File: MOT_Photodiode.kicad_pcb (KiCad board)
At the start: 2 copper layers, 32 x 25 mm, 18 parts, among them J1 Supply, J2 output, J3 photodiode, U1 LT3032-12, U2 ADA4898-1YRDZ

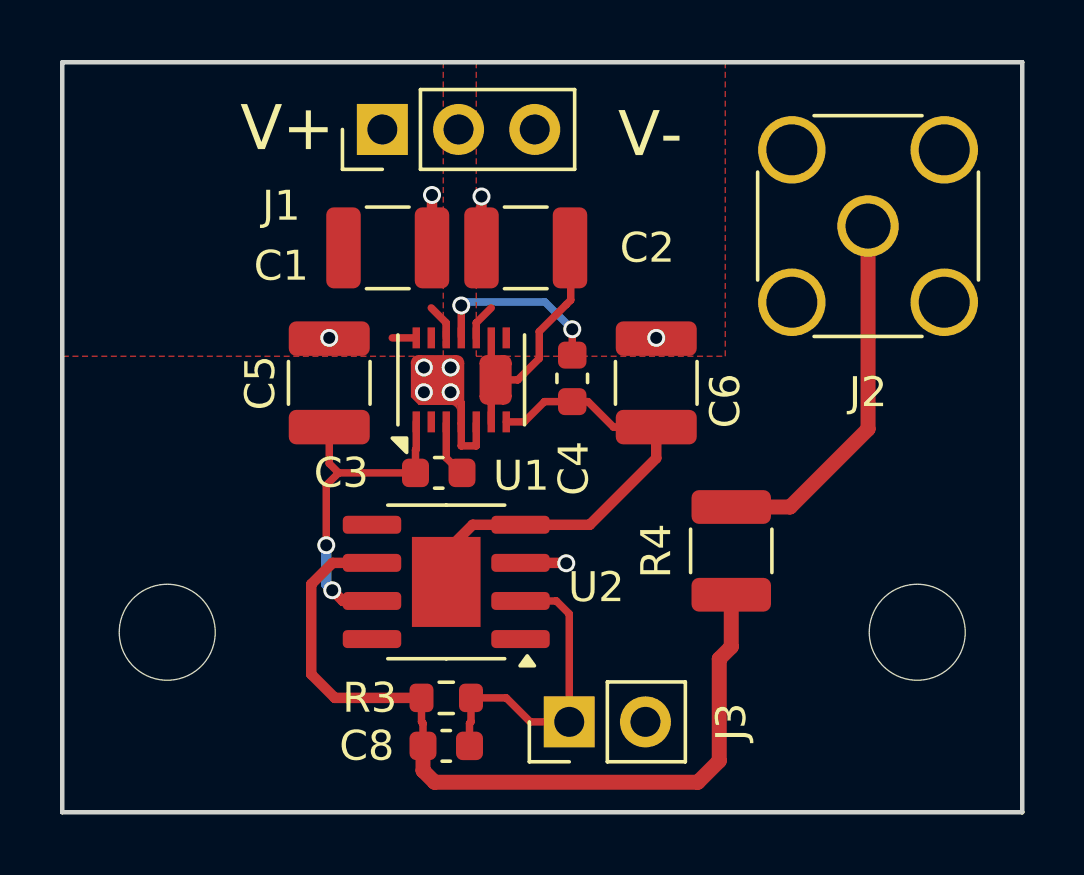
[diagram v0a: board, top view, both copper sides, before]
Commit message: Reduced via drill size from 0.4 mm to 0.3 mm
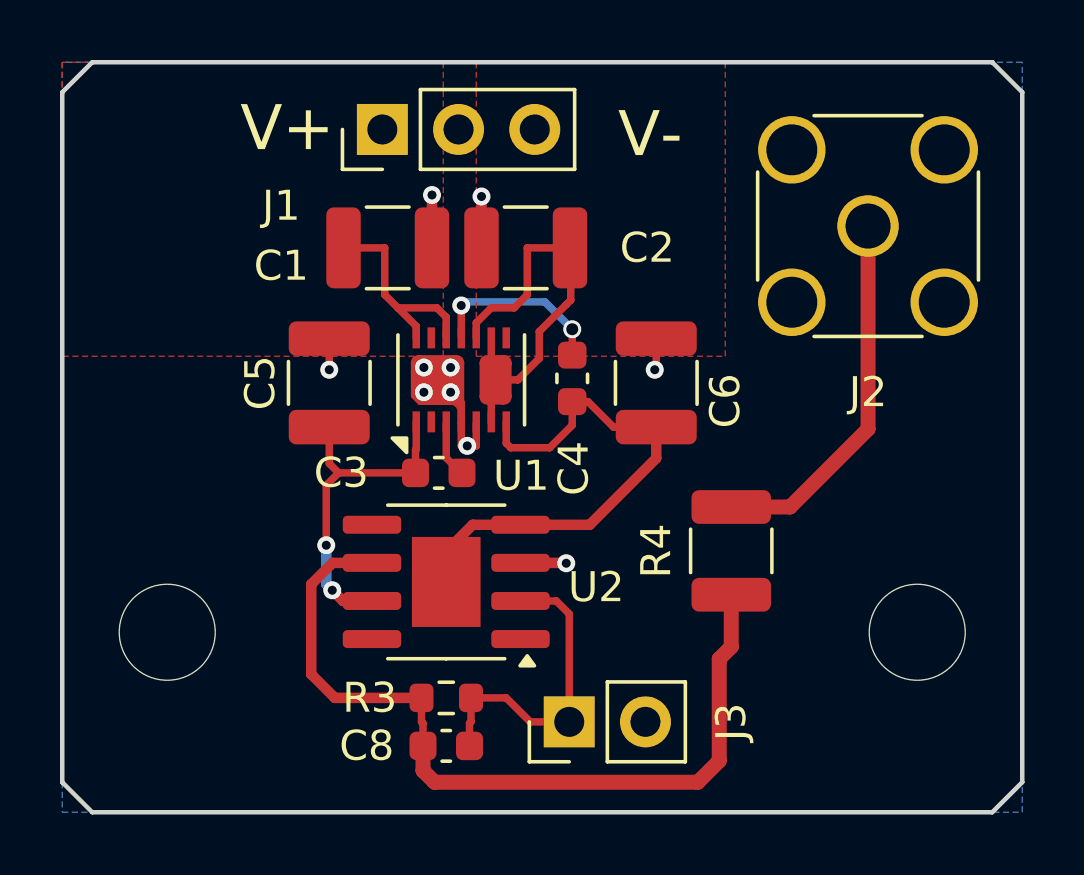
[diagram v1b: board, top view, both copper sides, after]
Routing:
- net +15V: track 2.01 -> 7.24 mm
- net -15V: track 8.37 -> 12.7 mm
- net GND: track 8.19 -> 10.3 mm, vias 9 -> 10
- net V-: track 16.0 -> 17.6 mm
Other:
- outline, holes or cut-outs redrawn
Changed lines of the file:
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@@
 	)
 	(gr_line
-		(start 127.45 112.25)
-		(end 159.45 112.25)
+		(start 128.45 112.25)
+		(end 158.45 112.25)
 		(stroke
 			(width 0.15)
@@
 	)
 	(gr_line
-		(start 159.45 112.25)
-		(end 159.45 87.25)
+		(start 159.45 111.25)
+		(end 159.45 88.25)
 		(stroke
 			(width 0.15)
@@
 	)
 	(gr_line
-		(start 159.45 87.25)
-		(end 127.45 87.25)
+		(start 159.45 88.25)
+		(end 158.45 87.25)
+		(stroke
+			(width 0.15)
+			(type default)
+		)
+		(layer "Edge.Cuts")
+	)
+	(gr_line
+		(start 158.45 87.25)
+		(end 128.45 87.25)
 		(stroke
 			(width 0.15)
@@
 	)
 	(gr_line
-		(start 127.45 87.25)
-		(end 127.45 112.25)
+		(start 127.45 88.25)
+		(end 127.45 111.25)
 		(stroke
 			(width 0.15)
 			(type solid)
+		)
+		(layer "Edge.Cuts")
+	)
+	(gr_line
+		(start 127.45 88.25)
+		(end 128.45 87.25)
+		(stroke
+			(width 0.15)
+			(type default)
+		)
+		(layer "Edge.Cuts")
+	)
+	(gr_line
+		(start 158.45 112.25)
+		(end 159.45 111.25)
+		(stroke
+			(width 0.15)
+			(type default)
+		)
+		(layer "Edge.Cuts")
+	)
+	(gr_line
+		(start 128.45 112.25)
+		(end 127.45 111.25)
+		(stroke
+			(width 0.15)
+			(type default)
 		)
 		(layer "Edge.Cuts")
@@
 	)
 	(segment
+		(start 147.2 97.5)
+		(end 147.25 97.45)
+		(width 0.25)
+		(layer "F.Cu")
+		(net 1)
+	)
+	(segment
+		(start 140.95 100.0375)
+		(end 141.25 100.0375)
+		(width 0.25)
+		(layer "F.Cu")
+		(net 1)
+	)
+	(segment
 		(start 140.75 99.2875)
 		(end 140.75 98.605)
@@
 	)
 	(segment
+		(start 147.25 97.45)
+		(end 147.25 96.4625)
+		(width 0.25)
+		(layer "F.Cu")
+		(net 1)
+	)
+	(segment
 		(start 144.2375 103.9375)
 		(end 144.25 103.95)
@@
 	)
 	(segment
+		(start 136.35 96.4625)
+		(end 136.35 97.5)
+		(width 0.25)
+		(layer "F.Cu")
+		(net 1)
+	)
+	(segment
 		(start 141.425 91.725)
 		(end 141.425 93.4375)
@@
 	(segment
 		(start 140.75 100.0375)
-		(end 141.25 100.0375)
+		(end 140.95 100.0375)
 		(width 0.25)
 		(layer "F.Cu")
@@
 		(at 139.505 97.425)
 		(size 0.6)
-		(drill 0.4)
+		(drill 0.3)
 		(layers "F.Cu" "B.Cu")
 		(net 1)
@@
 		(at 139.505 98.25)
 		(size 0.6)
-		(drill 0.4)
+		(drill 0.3)
 		(layers "F.Cu" "B.Cu")
 		(net 1)
@@
 		(at 144.25 103.95)
 		(size 0.6)
-		(drill 0.4)
+		(drill 0.3)
 		(layers "F.Cu" "B.Cu")
 		(net 1)
@@
 		(at 140.395 97.425)
 		(size 0.6)
-		(drill 0.4)
-		(layers "F.Cu" "B.Cu")
-		(net 1)
-	)
-	(via
-		(at 136.35 96.4375)
-		(size 0.6)
-		(drill 0.4)
+		(drill 0.3)
+		(layers "F.Cu" "B.Cu")
+		(net 1)
+	)
+	(via
+		(at 136.35 97.5)
+		(size 0.6)
+		(drill 0.3)
 		(layers "F.Cu" "B.Cu")
 		(net 1)
@@
 		(at 141.425 91.725)
 		(size 0.6)
-		(drill 0.4)
+		(drill 0.3)
+		(layers "F.Cu" "B.Cu")
+		(net 1)
+	)
+	(via
+		(at 140.95 100.0375)
+		(size 0.6)
+		(drill 0.3)
 		(layers "F.Cu" "B.Cu")
 		(net 1)
@@
 		(at 140.395 98.25)
 		(size 0.6)
-		(drill 0.4)
+		(drill 0.3)
 		(layers "F.Cu" "B.Cu")
 		(net 1)
@@
 		(at 139.775 91.675)
 		(size 0.6)
-		(drill 0.4)
-		(layers "F.Cu" "B.Cu")
-		(net 1)
-	)
-	(via
-		(at 147.25 96.4375)
-		(size 0.6)
-		(drill 0.4)
+		(drill 0.3)
+		(layers "F.Cu" "B.Cu")
+		(net 1)
+	)
+	(via
+		(at 147.2 97.5)
+		(size 0.6)
+		(drill 0.3)
 		(layers "F.Cu" "B.Cu")
 		(net 1)
@@
 		(at 136.45 104.85)
 		(size 0.6)
-		(drill 0.4)
+		(drill 0.3)
 		(layers "F.Cu" "B.Cu")
 		(net 2)
@@
 		(at 136.25 103.35)
 		(size 0.6)
-		(drill 0.4)
+		(drill 0.3)
 		(layers "F.Cu" "B.Cu")
 		(net 2)
@@
 	(segment
 		(start 142.25 99.2375)
-		(end 142.85 99.2375)
+		(end 142.25 99.95)
+		(width 0.25)
+		(layer "F.Cu")
+		(net 3)
+	)
+	(segment
+		(start 142.25 99.95)
+		(end 142.4 100.1)
+		(width 0.25)
+		(layer "F.Cu")
+		(net 3)
+	)
+	(segment
+		(start 143.7 100.1)
+		(end 144.45 99.35)
 		(width 0.25)
 		(layer "F.Cu")
@@
 	)
 	(segment
-		(start 142.85 99.2375)
-		(end 143.525 98.5625)
-		(width 0.25)
-		(layer "F.Cu")
-		(net 3)
-	)
-	(segment
 		(start 141.1325 102.6675)
 		(end 140.25 103.55)
@@
 	)
 	(segment
+		(start 144.45 99.35)
+		(end 144.45 98.5625)
+		(width 0.25)
+		(layer "F.Cu")
+		(net 3)
+	)
+	(segment
 		(start 147.25 100.45)
 		(end 147.25 99.4125)
@@
 	)
 	(segment
-		(start 143.525 98.5625)
-		(end 144.45 98.5625)
+		(start 142.4 100.1)
+		(end 143.7 100.1)
 		(width 0.25)
 		(layer "F.Cu")
@@
 		(at 140.75 95.357825)
 		(size 0.6)
-		(drill 0.4)
+		(drill 0.3)
 		(layers "F.Cu" "B.Cu")
 		(net 6)
@@
 	)
 	(segment
+		(start 140.25 95.75)
+		(end 139.9375 95.4375)
+		(width 0.25)
+		(layer "F.Cu")
+		(net 13)
+	)
+	(segment
 		(start 140.25 96.4375)
-		(end 140.25 95.9375)
+		(end 140.25 95.75)
 		(width 0.25)
 		(layer "F.Cu")
@@
 	)
 	(segment
-		(start 140.25 95.9375)
-		(end 139.75 95.4375)
+		(start 138.2 95)
+		(end 138.2 93.4375)
 		(width 0.25)
 		(layer "F.Cu")
@@
 	)
 	(segment
+		(start 138.2 93.4375)
+		(end 136.825 93.4375)
+		(width 0.25)
+		(layer "F.Cu")
+		(net 13)
+	)
+	(segment
+		(start 139.25 96.05)
+		(end 138.2 95)
+		(width 0.25)
+		(layer "F.Cu")
+		(net 13)
+	)
+	(segment
 		(start 139.25 96.4375)
-		(end 138.45 96.4375)
+		(end 139.25 96.05)
+		(width 0.25)
+		(layer "F.Cu")
+		(net 13)
+	)
+	(segment
+		(start 139.9375 95.4375)
+		(end 138.6375 95.4375)
 		(width 0.25)
 		(layer "F.Cu")
@@
 	)
 	(segment
+		(start 142.5125 95.4375)
+		(end 142.95 95)
+		(width 0.25)
+		(layer "F.Cu")
+		(net 14)
+	)
+	(segment
 		(start 144.25 95.3275)
 		(end 143.35 96.2275)
@@
 	)
 	(segment
+		(start 141.75 99.2875)
+		(end 141.75 97.9375)
+		(width 0.25)
+		(layer "F.Cu")
+		(net 14)
+	)
+	(segment
+		(start 142.95 93.4375)
+		(end 144.375 93.4375)
+		(width 0.25)
+		(layer "F.Cu")
+		(net 14)
+	)
+	(segment
+		(start 141.25 96.4375)
+		(end 141.25 95.9375)
+		(width 0.25)
+		(layer "F.Cu")
+		(net 14)
+	)
+	(segment
+		(start 143.35 97.1225)
+		(end 142.635 97.8375)
+		(width 0.25)
+		(layer "F.Cu")
+		(net 14)
+	)
+	(segment
+		(start 142.95 95)
+		(end 142.95 93.4375)
+		(width 0.25)
+		(layer "F.Cu")
+		(net 14)
+	)
+	(segment
+		(start 144.4 95.1775)
+		(end 144.25 95.3275)
+		(width 0.25)
+		(layer "F.Cu")
+		(net 14)
+	)
+	(segment
 		(start 141.25 95.9375)
 		(end 141.75 95.4375)
@@
 	)
 	(segment
-		(start 141.75 99.2875)
-		(end 141.75 97.9375)
-		(width 0.25)
-		(layer "F.Cu")
-		(net 14)
-	)
-	(segment
-		(start 143.35 97.1225)
-		(end 142.635 97.8375)
-		(width 0.25)
-		(layer "F.Cu")
-		(net 14)
-	)
-	(segment
-		(start 144.4 95.1775)
-		(end 144.25 95.3275)
-		(width 0.25)
-		(layer "F.Cu")
-		(net 14)
-	)
-	(segment
-		(start 141.25 96.4375)
-		(end 141.25 95.9375)
-		(width 0.25)
-		(layer "F.Cu")
-		(net 14)
-	)
-	(segment
 		(start 143.35 96.2275)
 		(end 143.35 97.1225)
@@
 		(start 141.75 97.9375)
 		(end 141.85 97.8375)
+		(width 0.25)
+		(layer "F.Cu")
+		(net 14)
+	)
+	(segment
+		(start 141.75 95.4375)
+		(end 142.5125 95.4375)
 		(width 0.25)
 		(layer "F.Cu")
@@
 			(thermal_gap 0.508)
 			(thermal_bridge_width 0.508)
+			(smoothing chamfer)
+			(radius 0.5)
 		)
 		(polygon
@@
 		(min_thickness 0.254)
 		(filled_areas_thickness no)
-		(fill
+		(fill yes
 			(thermal_gap 0.508)
 			(thermal_bridge_width 0.508)
+			(smoothing chamfer)
+			(radius 0.5)
 		)
 		(polygon

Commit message: Added teardrops
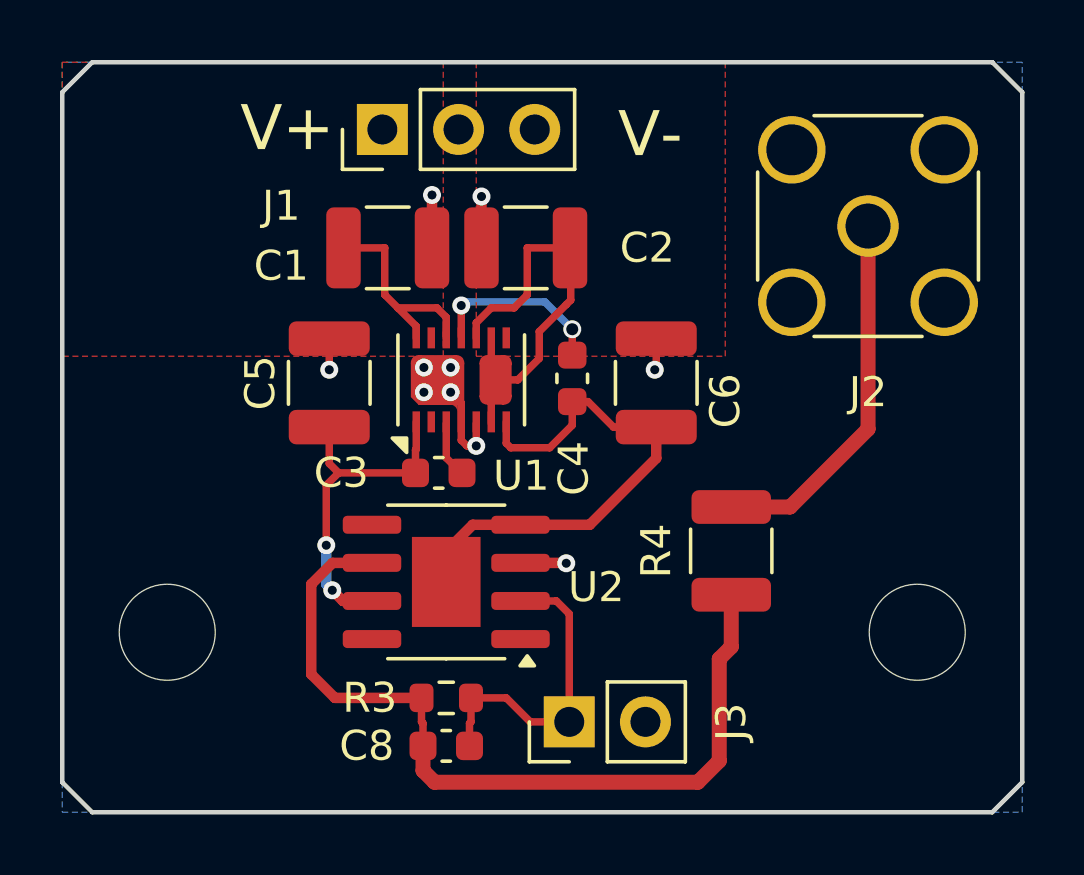
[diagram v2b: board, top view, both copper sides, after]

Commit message: Added BOM
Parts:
- R4: value 49.9 -> 49.9R

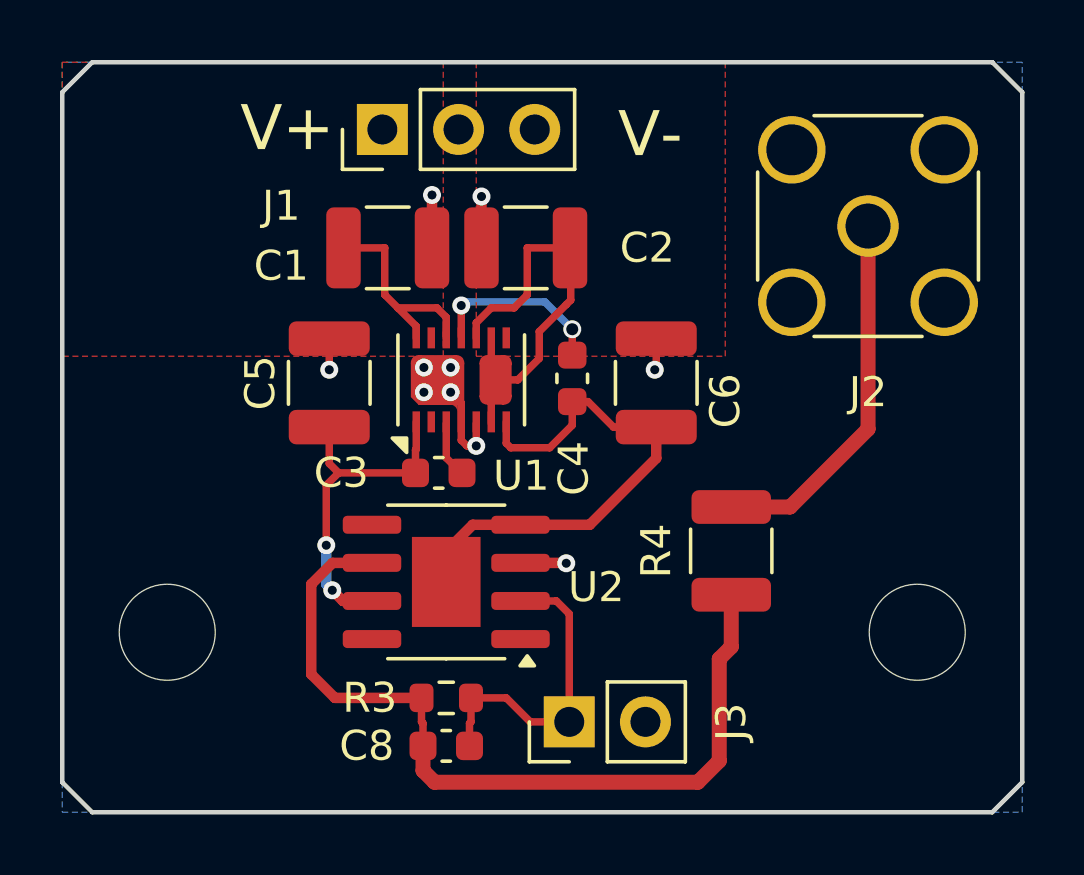
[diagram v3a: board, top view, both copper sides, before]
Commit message: Update/kicad9 (#2)
* Update files to KiCad 9 incl. footprint updates

* Bump CI to KiCad 9

* Refilled copper pour

* Bump version to 1.1.1
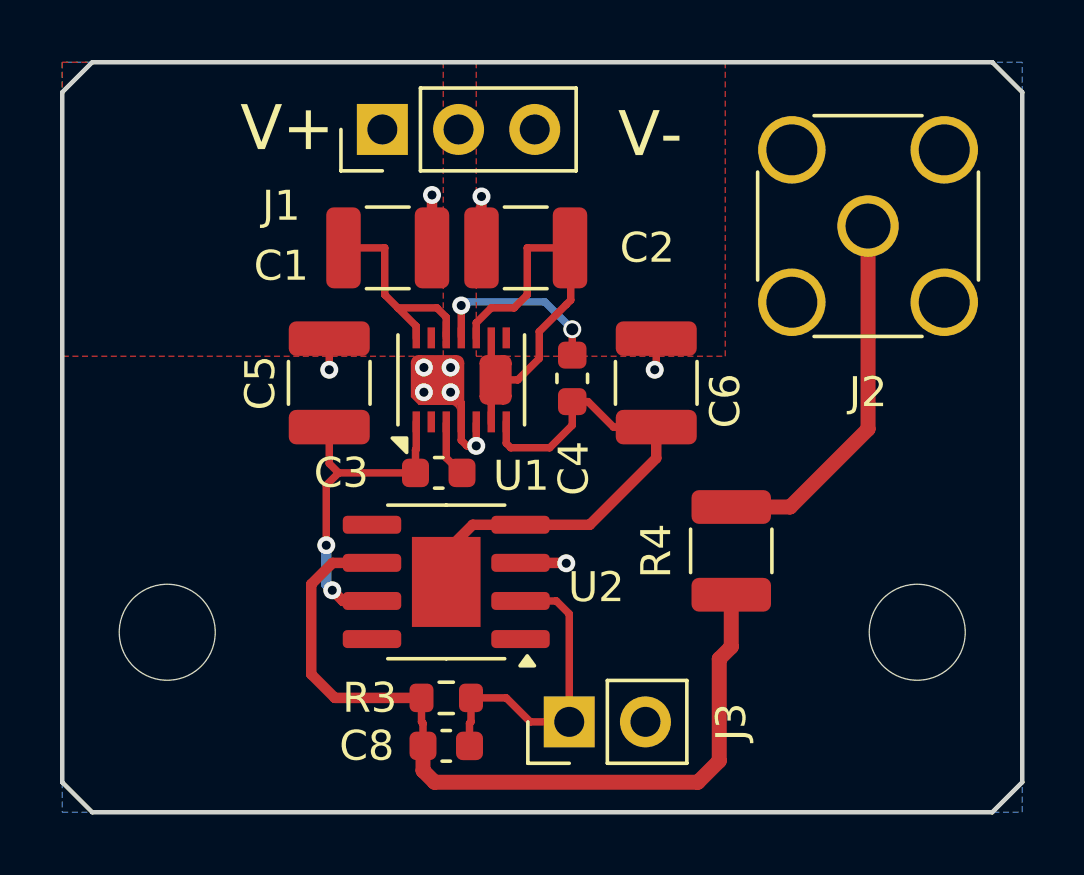
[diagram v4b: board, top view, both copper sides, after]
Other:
- board text added: "MOT_photodiode 1.1.1 Design: T. Preuschoff Date: 2025-06 https://github.com/ TU-Darmstadt-APQ"
- board text removed: "MOT_photodiode 1.1.0 Design: T. Preuschoff Date: 2025-02 https://github.com/ TU-Darmstadt-APQ"
